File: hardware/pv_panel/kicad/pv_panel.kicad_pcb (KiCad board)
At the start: 2 copper layers, 82.5 x 98 mm, 23 parts, among them P1 S2B-PH-SM4-TB(LF)(SN)

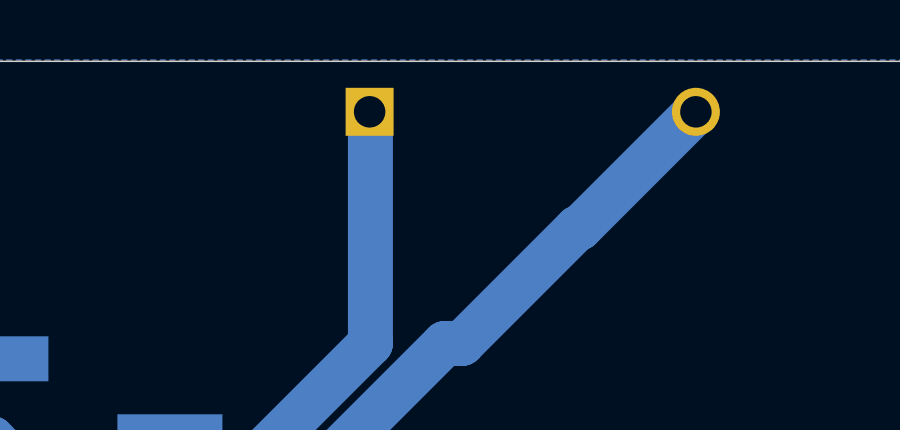
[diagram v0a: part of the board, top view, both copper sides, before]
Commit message: Mount through-hole D1 on the outside solar-cell face
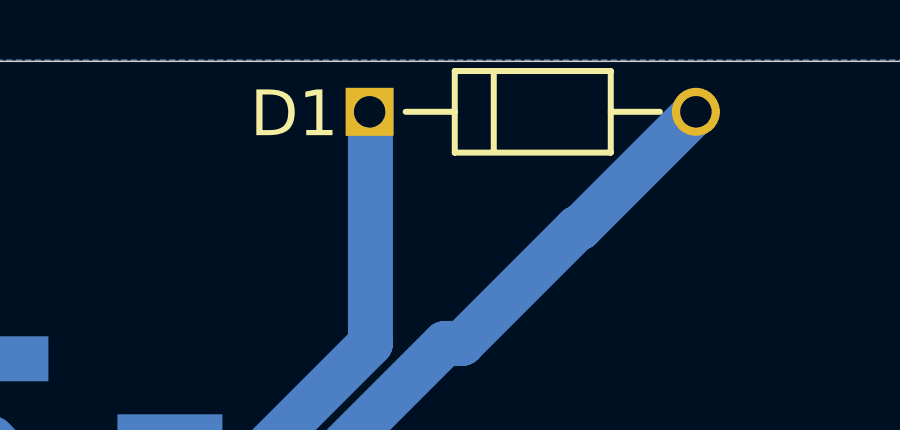
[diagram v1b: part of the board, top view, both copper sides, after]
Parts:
- D1: moved to F.Cu
